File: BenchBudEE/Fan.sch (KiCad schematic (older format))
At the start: 0 parts

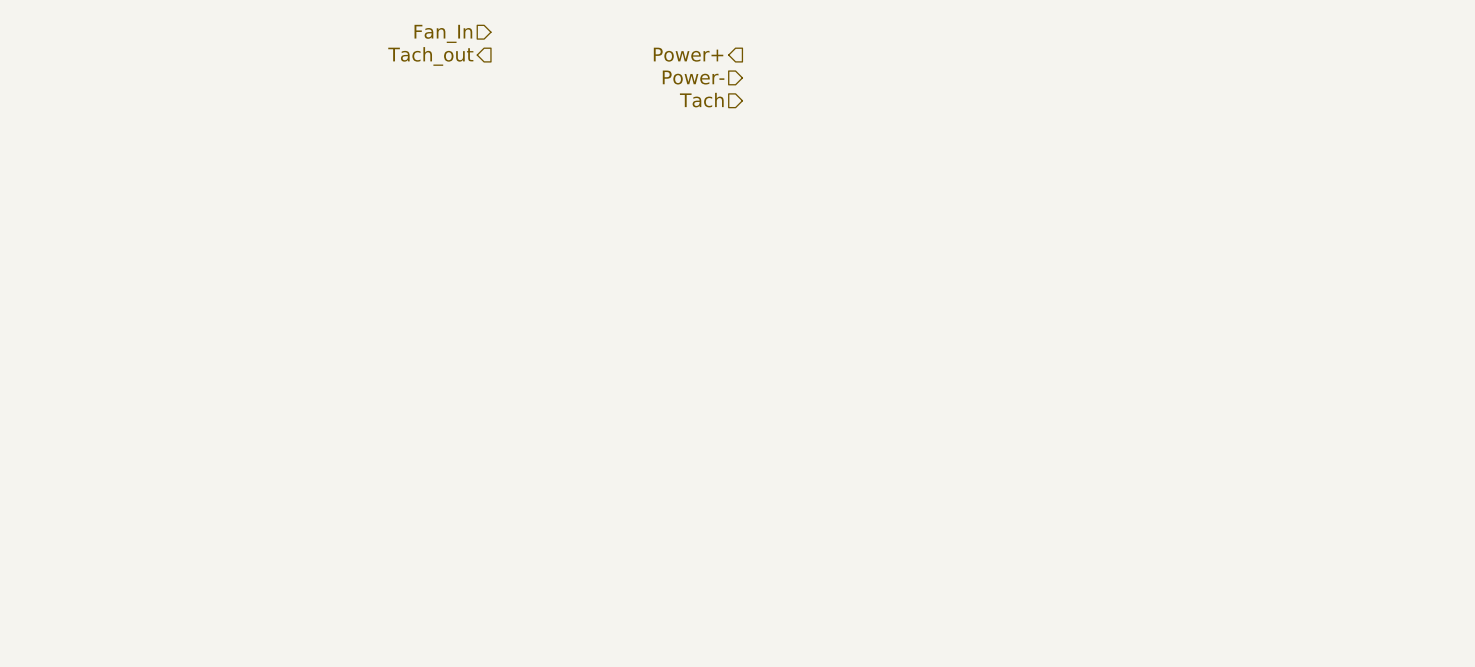
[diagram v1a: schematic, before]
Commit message: Implementing Current / Fan Driver schematic
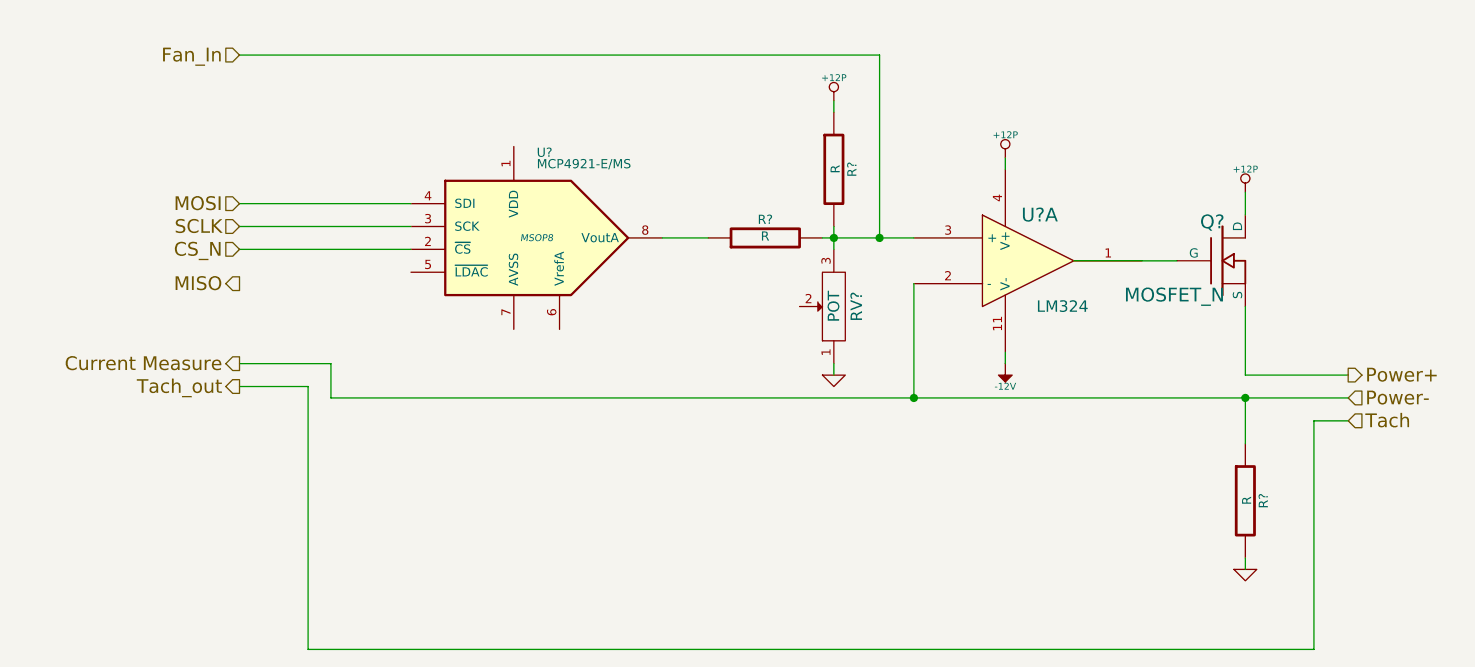
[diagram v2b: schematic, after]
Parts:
- added Q?: MOSFET_N, ~, symbol MOSFET_N
- added R? (x3): R, ~, symbol R
- added RV?: POT, ~, symbol POT
- added U?: LM324, symbol LM324
- added U?: MCP4921-E/MS, MSOP8, symbol MCP4921-E/MS
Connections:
- net labels added: +12P, -12V, CS_N, Current Measure, GND, MISO, MOSI, SCLK
- wire segments 0 -> 27
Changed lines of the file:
@@
 Sheet 7 8
 Title ""
-Date "9 feb 2014"
+Date "10 feb 2014"
 Rev ""
 Comp ""
@@
 Comment4 ""
 $EndDescr
-Text HLabel 4600 2850 0    60   Output ~ 0
+Text HLabel 7250 4250 2    60   Output ~ 0
 Power+
-Text HLabel 4600 2950 0    60   Input ~ 0
+Text HLabel 7250 4350 2    60   Input ~ 0
 Power-
-Text HLabel 4600 3050 0    60   Input ~ 0
+Text HLabel 7250 4450 2    60   Input ~ 0
 Tach
-Text HLabel 3500 2850 0    60   Output ~ 0
+Text HLabel 2400 4300 0    60   Output ~ 0
 Tach_out
-Text HLabel 3500 2750 0    60   Input ~ 0
+Text HLabel 2400 2850 0    60   Input ~ 0
 Fan_In
+$Comp
+L LM324 U?
+U 1 1 52F82C69
+P 5850 3750
+F 0 "U?" H 5900 3950 60  0000 C CNN
+F 1 "LM324" H 6000 3550 50  0000 C CNN
+F 2 "" H 5850 3750 60  0000 C CNN
+F 3 "" H 5850 3750 60  0000 C CNN
+	1    5850 3750
+	1    0    0    -1
+$EndComp
+$Comp
+L MOSFET_N Q?
+U 1 1 52F82C78
+P 6700 3750
+F 0 "Q?" H 6710 3920 60  0000 R CNN
+F 1 "MOSFET_N" H 6710 3600 60  0000 R CNN
+F 2 "~" H 6700 3750 60  0000 C CNN
+F 3 "~" H 6700 3750 60  0000 C CNN
+	1    6700 3750
+	1    0    0    -1
+$EndComp
+$Comp
+L +12P #PWR?
+U 1 1 52F82C87
+P 6800 3450
+F 0 "#PWR?" H 6800 3420 30  0001 C CNN
+F 1 "+12P" H 6800 3550 30  0000 C CNN
+F 2 "" H 6800 3450 60  0000 C CNN
+F 3 "" H 6800 3450 60  0000 C CNN
+	1    6800 3450
+	1    0    0    -1
+$EndComp
+Wire Wire Line
+	6050 3750 6500 3750
+Wire Wire Line
+	6800 3950 6800 4250
+Wire Wire Line
+	6800 4250 7250 4250
+$Comp
+L R R?
+U 1 1 52F82CA6
+P 6800 4800
+F 0 "R?" V 6880 4800 40  0000 C CNN
+F 1 "R" V 6807 4801 40  0000 C CNN
+F 2 "~" V 6730 4800 30  0000 C CNN
+F 3 "~" H 6800 4800 30  0000 C CNN
+	1    6800 4800
+	1    0    0    -1
+$EndComp
+$Comp
+L GND #PWR?
+U 1 1 52F82CB5
+P 6800 5100
+F 0 "#PWR?" H 6800 5100 30  0001 C CNN
+F 1 "GND" H 6800 5030 30  0001 C CNN
+F 2 "" H 6800 5100 60  0000 C CNN
+F 3 "" H 6800 5100 60  0000 C CNN
+	1    6800 5100
+	1    0    0    -1
+$EndComp
+Wire Wire Line
+	6800 5050 6800 5100
+Wire Wire Line
+	6800 4350 6800 4550
+Wire Wire Line
+	5350 4350 5350 3850
+Connection ~ 6800 4350
+Wire Wire Line
+	6800 3450 6800 3550
+$Comp
+L +12P #PWR?
+U 1 1 52F82CEF
+P 5750 3300
+F 0 "#PWR?" H 5750 3270 30  0001 C CNN
+F 1 "+12P" H 5750 3400 30  0000 C CNN
+F 2 "" H 5750 3300 60  0000 C CNN
+F 3 "" H 5750 3300 60  0000 C CNN
+	1    5750 3300
+	1    0    0    -1
+$EndComp
+Wire Wire Line
+	5750 3300 5750 3350
+$Comp
+L -12V #PWR?
+U 1 1 52F82D01
+P 5750 4200
+F 0 "#PWR?" H 5750 4330 20  0001 C CNN
+F 1 "-12V" H 5750 4300 30  0000 C CNN
+F 2 "" H 5750 4200 60  0000 C CNN
+F 3 "" H 5750 4200 60  0000 C CNN
+	1    5750 4200
+	-1   0    0    1
+$EndComp
+Wire Wire Line
+	5750 4150 5750 4200
+$Comp
+L R R?
+U 1 1 52F82D19
+P 5000 3350
+F 0 "R?" V 5080 3350 40  0000 C CNN
+F 1 "R" V 5007 3351 40  0000 C CNN
+F 2 "~" V 4930 3350 30  0000 C CNN
+F 3 "~" H 5000 3350 30  0000 C CNN
+	1    5000 3350
+	1    0    0    -1
+$EndComp
+$Comp
+L POT RV?
+U 1 1 52F82D2B
+P 5000 3950
+F 0 "RV?" H 5000 3850 50  0000 C CNN
+F 1 "POT" H 5000 3950 50  0000 C CNN
+F 2 "~" H 5000 3950 60  0000 C CNN
+F 3 "~" H 5000 3950 60  0000 C CNN
+	1    5000 3950
+	0    -1   -1   0
+$EndComp
+$Comp
+L +12P #PWR?
+U 1 1 52F82D42
+P 5000 3050
+F 0 "#PWR?" H 5000 3020 30  0001 C CNN
+F 1 "+12P" H 5000 3150 30  0000 C CNN
+F 2 "" H 5000 3050 60  0000 C CNN
+F 3 "" H 5000 3050 60  0000 C CNN
+	1    5000 3050
+	1    0    0    -1
+$EndComp
+Wire Wire Line
+	5000 3050 5000 3100
+Wire Wire Line
+	5000 3600 5000 3700
+Connection ~ 5000 3650
+$Comp
+L GND #PWR?
+U 1 1 52F82D6F
+P 5000 4250
+F 0 "#PWR?" H 5000 4250 30  0001 C CNN
+F 1 "GND" H 5000 4180 30  0001 C CNN
+F 2 "" H 5000 4250 60  0000 C CNN
+F 3 "" H 5000 4250 60  0000 C CNN
+	1    5000 4250
+	1    0    0    -1
+$EndComp
+Wire Wire Line
+	5000 4200 5000 4250
+$Comp
+L MCP4921-E/MS U?
+U 1 1 52F82D97
+P 3700 3650
+F 0 "U?" H 3700 4000 40  0000 L BNN
+F 1 "MCP4921-E/MS" H 3700 3950 40  0000 L BNN
+F 2 "MSOP8" H 3700 3650 30  0000 C CIN
+F 3 "" H 3700 3650 60  0000 C CNN
+	1    3700 3650
+	1    0    0    -1
+$EndComp
+Text HLabel 2400 4200 0    60   Output ~ 0
+Current Measure
+Wire Wire Line
+	7250 4450 7100 4450
+Wire Wire Line
+	7100 4450 7100 5450
+Wire Wire Line
+	7100 5450 2700 5450
+Wire Wire Line
+	2700 5450 2700 4300
+Wire Wire Line
+	2700 4300 2400 4300
+Wire Wire Line
+	2800 4350 2800 4200
+Wire Wire Line
+	2800 4200 2400 4200
+Connection ~ 5350 4350
+Wire Wire Line
+	2800 4350 7250 4350
+Wire Wire Line
+	2400 2850 5200 2850
+Connection ~ 5200 3650
+Wire Wire Line
+	4950 3650 5350 3650
+$Comp
+L R R?
+U 1 1 52F82EA4
+P 4700 3650
+F 0 "R?" V 4780 3650 40  0000 C CNN
+F 1 "R" V 4707 3651 40  0000 C CNN
+F 2 "~" V 4630 3650 30  0000 C CNN
+F 3 "~" H 4700 3650 30  0000 C CNN
+	1    4700 3650
+	0    -1   -1   0
+$EndComp
+Wire Wire Line
+	4450 3650 4250 3650
+Text HLabel 2400 3500 0    60   Input ~ 0
+MOSI
+Text HLabel 2400 3850 0    60   Output ~ 0
+MISO
+Text HLabel 2400 3600 0    60   Input ~ 0
+SCLK
+Text HLabel 2400 3700 0    60   Input ~ 0
+CS_N
+Wire Wire Line
+	5200 2850 5200 3650
+Wire Wire Line
+	3150 3500 2400 3500
+Wire Wire Line
+	3150 3600 2400 3600
+Wire Wire Line
+	3150 3700 2400 3700
 $EndSCHEMATC
